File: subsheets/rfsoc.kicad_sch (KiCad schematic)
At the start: 27 parts, among them U1 nRF54L15-QFXX, U2 ADXL367BCCZ-RL7, X2 32MHz

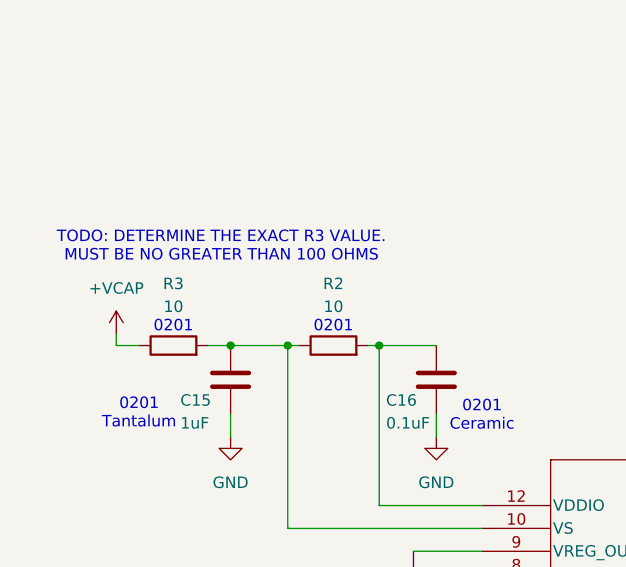
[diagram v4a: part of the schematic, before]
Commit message: changed resistor to ferrite bead for accel power filtering
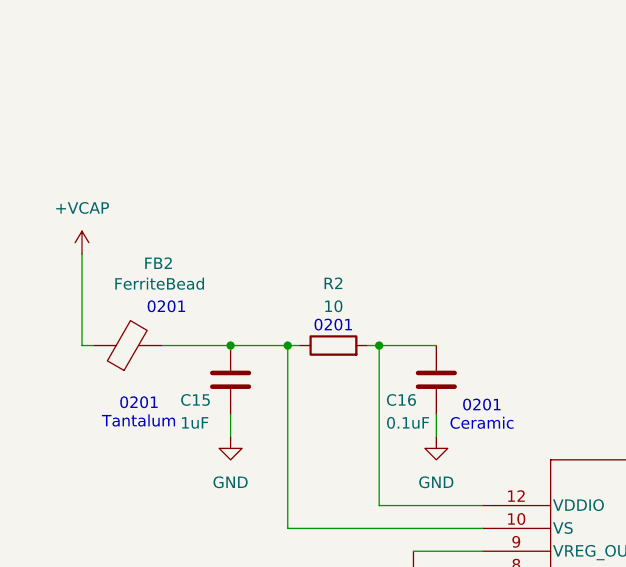
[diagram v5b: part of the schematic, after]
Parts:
- removed R3: 10, symbol Device:R
- added FB2: FerriteBead, symbol Device:FerriteBead
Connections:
- net +VCAP: now also FB2.1
- net at C15.1, R2.1, U2.10 (VS): now also FB2.2
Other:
- note removed: "TODO: DETERMINE THE EXACT R3 VALUE. MUST BE NO GREATER THAN 100 OHMS"
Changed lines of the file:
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@@
 	(wire
 		(pts
-			(xy 30.48 105.41) (xy 30.48 106.68)
+			(xy 26.67 96.52) (xy 26.67 106.68)
 		)
 		(stroke
@@
 	(wire
 		(pts
-			(xy 30.48 106.68) (xy 33.02 106.68)
+			(xy 26.67 106.68) (xy 27.94 106.68)
 		)
 		(stroke
@@
 	(wire
 		(pts
-			(xy 40.64 106.68) (xy 43.18 106.68)
+			(xy 35.56 106.68) (xy 43.18 106.68)
 		)
 		(stroke
@@
 		)
 	)
-	(text "0201\n"
+	(text "XTAL_2016\n"
 		(exclude_from_sim no)
-		(at 36.83 104.648 0)
+		(at 212.344 70.866 0)
 		(effects
 			(font
@@
 		)
 	)
-	(text "XTAL_2016\n"
+	(text "0201\n"
 		(exclude_from_sim no)
-		(at 212.344 70.866 0)
+		(at 259.08 43.688 0)
 		(effects
 			(font
@@
 	(text "0201\n"
 		(exclude_from_sim no)
-		(at 259.08 43.688 0)
+		(at 36.068 102.616 0)
 		(effects
 			(font
@@
 		)
 	)
-	(text "TODO: DETERMINE THE EXACT R3 VALUE. \nMUST BE NO GREATER THAN 100 OHMS\n"
-		(exclude_from_sim no)
-		(at 42.164 95.758 0)
-		(effects
-			(font
-				(size 1.27 1.27)
-			)
-		)
-	)
 	(text "0201\n"
 		(exclude_from_sim no)
@@
 	)
 	(symbol
-		(lib_id "Device:R")
-		(at 36.83 106.68 90)
-		(unit 1)
-		(exclude_from_sim no)
-		(in_bom yes)
-		(on_board yes)
-		(dnp no)
-		(property "Reference" "R3"
-			(at 36.83 99.822 90)
-			(effects
-				(font
-					(size 1.27 1.27)
-				)
-			)
-		)
-		(property "Value" "10"
-			(at 36.83 102.362 90)
-			(effects
-				(font
-					(size 1.27 1.27)
-				)
-			)
-		)
-		(property "Footprint" ""
-			(at 36.83 108.458 90)
-			(effects
-				(font
-					(size 1.27 1.27)
-				)
-				(hide yes)
-			)
-		)
-		(property "Datasheet" "~"
-			(at 36.83 106.68 0)
-			(effects
-				(font
-					(size 1.27 1.27)
-				)
-				(hide yes)
-			)
-		)
-		(property "Description" "Resistor"
-			(at 36.83 106.68 0)
-			(effects
-				(font
-					(size 1.27 1.27)
-				)
-				(hide yes)
-			)
-		)
-		(pin "1"
-		)
-		(pin "2"
-		)
-		(instances
-			(project "earworm_hardware"
-				(path "/881910d0-5a86-41d0-856d-d1bf2648669f/775ed5aa-f2a7-4007-b181-21772bd09852"
-					(reference "R3")
-					(unit 1)
-				)
-			)
-		)
-	)
-	(symbol
 		(lib_id "power:GND")
 		(at 204.47 85.09 0)
@@
 	)
 	(symbol
+		(lib_id "Device:FerriteBead")
+		(at 31.75 106.68 90)
+		(unit 1)
+		(exclude_from_sim no)
+		(in_bom yes)
+		(on_board yes)
+		(dnp no)
+		(property "Reference" "FB2"
+			(at 36.83 97.5869 90)
+			(effects
+				(font
+					(size 1.27 1.27)
+				)
+				(justify left)
+			)
+		)
+		(property "Value" "FerriteBead"
+			(at 40.386 99.8729 90)
+			(effects
+				(font
+					(size 1.27 1.27)
+				)
+				(justify left)
+			)
+		)
+		(property "Footprint" ""
+			(at 31.75 108.458 90)
+			(effects
+				(font
+					(size 1.27 1.27)
+				)
+				(hide yes)
+			)
+		)
+		(property "Datasheet" "~"
+			(at 31.75 106.68 0)
+			(effects
+				(font
+					(size 1.27 1.27)
+				)
+				(hide yes)
+			)
+		)
+		(property "Description" "Ferrite bead"
+			(at 31.75 106.68 0)
+			(effects
+				(font
+					(size 1.27 1.27)
+				)
+				(hide yes)
+			)
+		)
+		(pin "1"
+		)
+		(pin "2"
+		)
+		(instances
+			(project "earworm_hardware"
+				(path "/881910d0-5a86-41d0-856d-d1bf2648669f/775ed5aa-f2a7-4007-b181-21772bd09852"
+					(reference "FB2")
+					(unit 1)
+				)
+			)
+		)
+	)
+	(symbol
 		(lib_id "power:GND")
 		(at 68.58 139.7 0)
@@
 	(symbol
 		(lib_id "power:+1V0")
-		(at 30.48 105.41 0)
+		(at 26.67 96.52 0)
 		(unit 1)
 		(exclude_from_sim no)
@@
 		(fields_autoplaced yes)
 		(property "Reference" "#PWR021"
-			(at 30.48 109.22 0)
+			(at 26.67 100.33 0)
 			(effects
 				(font
@@
 		)
 		(property "Value" "+VCAP"
-			(at 30.48 100.33 0)
+			(at 26.67 91.44 0)
 			(effects
 				(font
@@
 		)
 		(property "Footprint" ""
-			(at 30.48 105.41 0)
+			(at 26.67 96.52 0)
 			(effects
 				(font
@@
 		)
 		(property "Datasheet" ""
-			(at 30.48 105.41 0)
+			(at 26.67 96.52 0)
 			(effects
 				(font
@@
 		)
 		(property "Description" "Power symbol creates a global label with name \"+1V0\""
-			(at 30.48 105.41 0)
+			(at 26.67 96.52 0)
 			(effects
 				(font

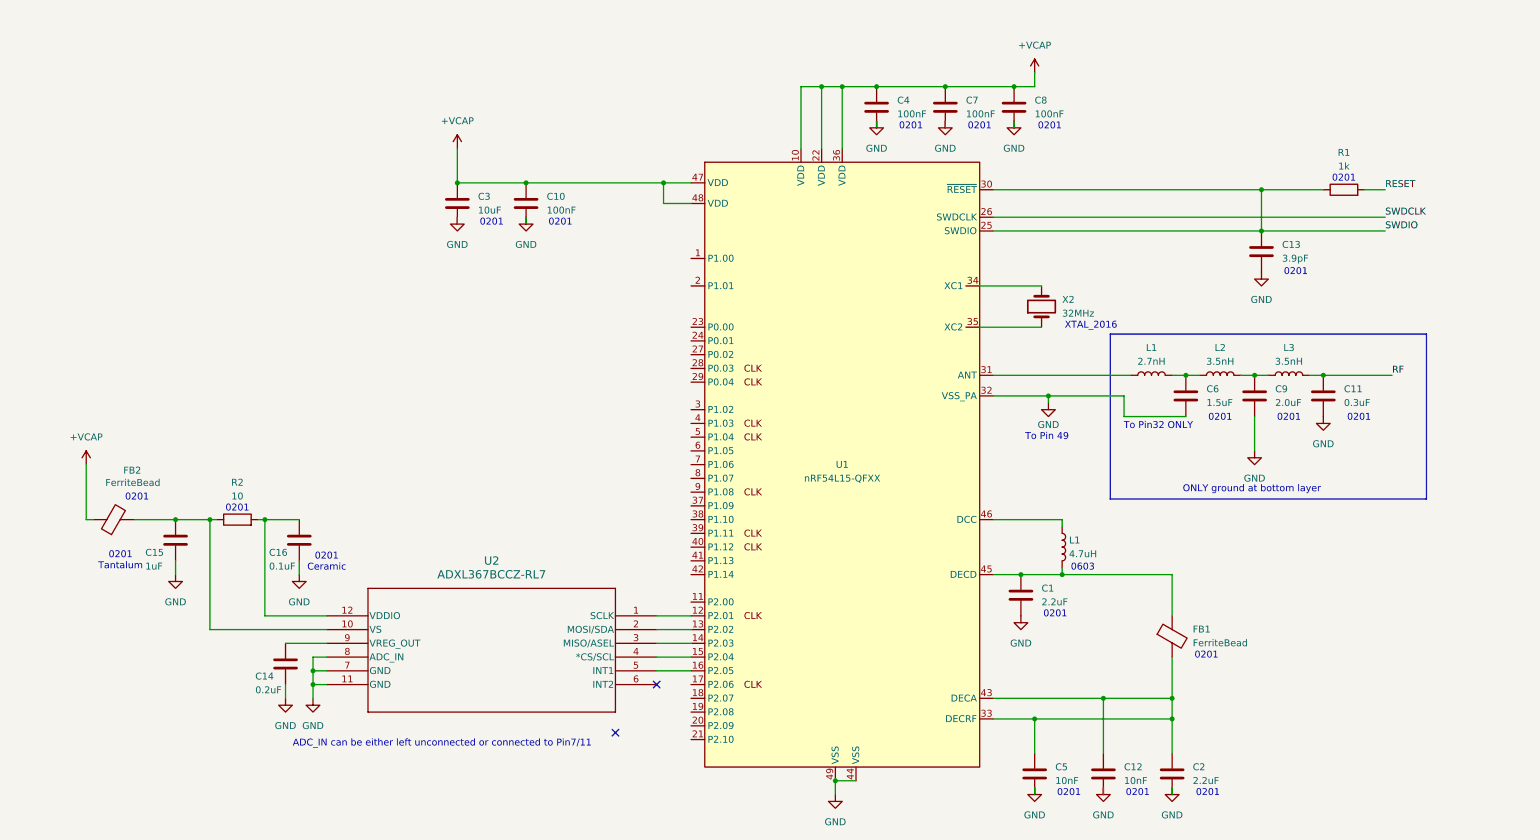
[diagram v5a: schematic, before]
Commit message: Added first draft of thermal energy harvesting chain. Need to run through ERC and fix errors
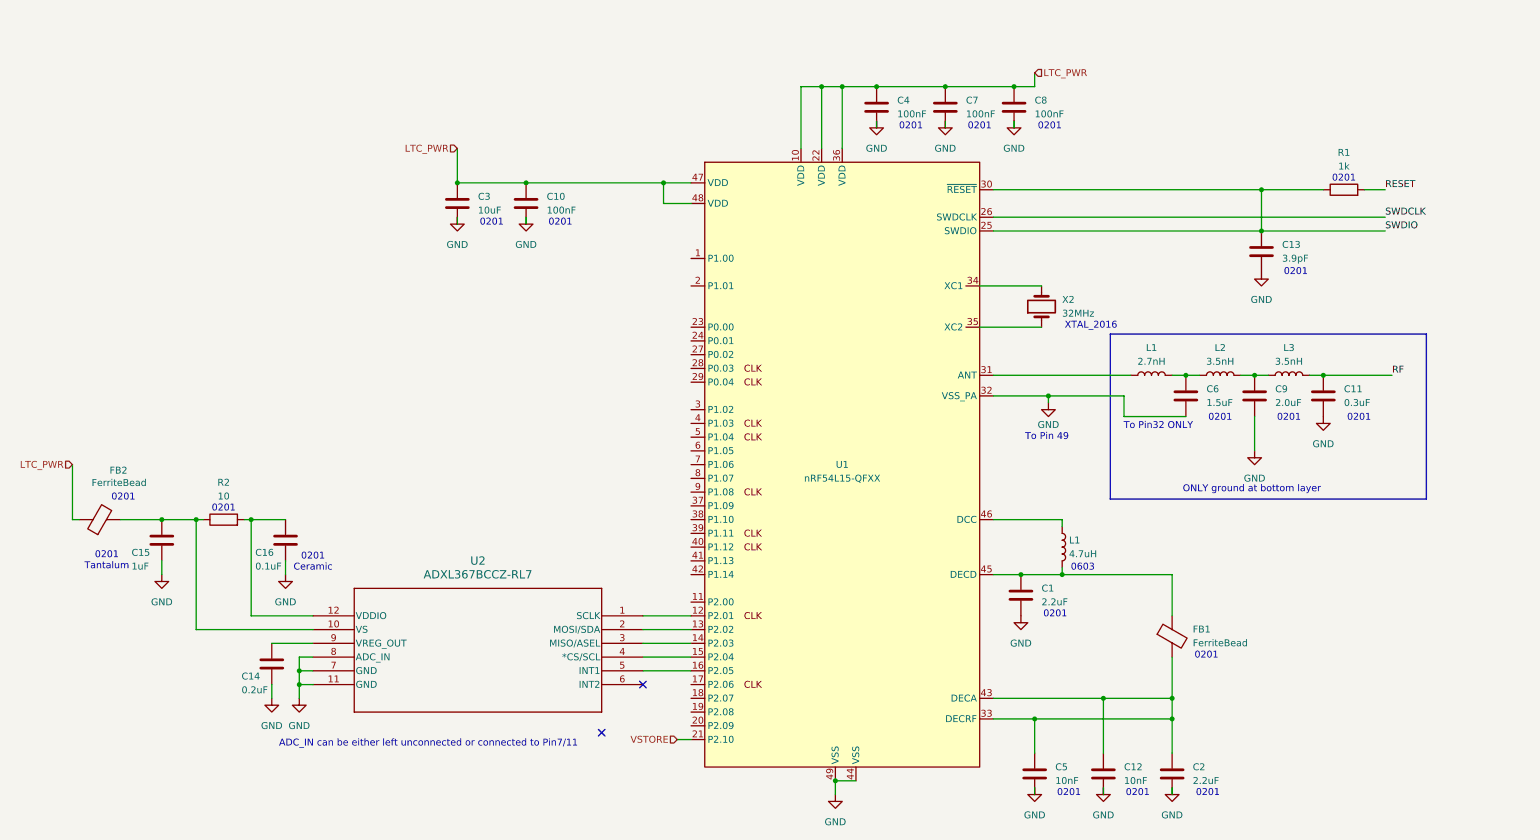
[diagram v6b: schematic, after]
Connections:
- net VSTORE: now reaches U1.21 (P2.10)
- net +VCAP renamed LTC_PWR
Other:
- moved on the sheet: C14, C15, C16, FB2, R2, U2

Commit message: Finished Schematic
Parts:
- removed C1: 2.2uF, symbol Device:C
- removed C2: 2.2uF, 0603, symbol Device:C
- removed C4, C7: 100nF, 0603, symbol Device:C
- removed C5: 10nF, 0603, symbol Device:C
- removed FB2: FerriteBead, symbol Device:FerriteBead
- removed L3: 3.5nH, symbol Device:L
- removed R1: 1k, symbol Device:R
- added C13, C9: 0.1uF, Capacitor_SMD:C_0603_1608Metric, symbol Device:C
- added C18: 10nF, Capacitor_SMD:C_0603_1608Metric, symbol Device:C
- added C19: 2.2uF, Capacitor_SMD:C_0603_1608Metric, symbol Device:C
- added C7: 1uF, Capacitor_SMD:C_0603_1608Metric_Pad1.08x0.95mm_HandSolder, symbol Device:C_Polarized
- added FB1: 75 @ 100MHz, Inductor_SMD:L_0603_1608Metric, symbol Device:FerriteBead
- added J2: Conn_01x05, Connector_PinHeader_1.00mm:PinHeader_1x05_P1.00mm_Vertical, symbol Connector_Generic:Conn_01x05
- added L4: 3.5nH, Inductor_SMD:L_0201_0603Metric, symbol Device:L
- added R2: 1k, Resistor_SMD:R_0603_1608Metric_Pad0.98x0.95mm_HandSolder, symbol Device:R_US
- C10: value 100nF -> 0.1uF; footprint 0603 -> Capacitor_SMD:C_0603_1608Metric; Part (none) -> CL10B104KB8NNNC; Tolerance (none) -> 10%; Voltage (none) -> 50V
- C11: renamed from C3; footprint 0603 -> Capacitor_SMD:C_0603_1608Metric; Part (none) -> CL10A106KQ8NNNC; Tolerance (none) -> 10%; Voltage (none) -> 6.3V
- C12: value 10nF -> 0.1uF; footprint 0603 -> Capacitor_SMD:C_0603_1608Metric; Part (none) -> CL10B104KB8NNNC; Tolerance (none) -> 10%; Voltage (none) -> 50V
- C14: value 0.2uF -> 0.1uF; footprint (none) -> Capacitor_SMD:C_0603_1608Metric; Part (none) -> CL10B104KB8NNNC; Tolerance (none) -> 10%; Voltage (none) -> 50V
- C15: value 1uF -> 2.2uF; footprint (none) -> Capacitor_SMD:C_0603_1608Metric; Part (none) -> CL10A225KO8NNNC; Tolerance (none) -> 10%; Voltage (none) -> 16V
- C16: value 0.1uF -> 10nF; footprint (none) -> Capacitor_SMD:C_0603_1608Metric; Part (none) -> CL10B103KB8NNNC; Tolerance (none) -> 10%; Voltage (none) -> 50V
- C17: renamed from C13; value 3.9pF -> 4pF; footprint (none) -> Capacitor_SMD:C_0603_1608Metric; Part (none) -> CL10C040CB8NNNC; Tolerance (none) -> 6.25%; Voltage (none) -> 50V
- C20: renamed from C6; value 1.5uF -> 1.5pF; footprint 0603 -> Capacitor_SMD:C_0201_0603Metric; Part (none) -> GJM0335C1E1R5WB01D
- C21: renamed from C9; value 2.0uF -> 2.0pF; footprint 0603 -> Capacitor_SMD:C_0201_0603Metric; Part (none) -> GJM0335C1E2R0WB01D
- C22: renamed from C11; value 0.3uF -> 0.3pF; footprint 0603 -> Capacitor_SMD:C_0201_0603Metric; Part (none) -> GJM0335C1ER30WB01D
- C8: value 100nF -> 0.22uF; footprint 0603 -> Capacitor_SMD:C_0603_1608Metric; Part (none) -> CL10B224KO8NNNC; Tolerance (none) -> 10%; Voltage (none) -> 16V
- FB2: renamed from FB1; value FerriteBead -> 120 @ 100MHz; footprint (none) -> Inductor_SMD:L_0603_1608Metric; Part (none) -> BLM18KG121TN1D
- L1: footprint (none) -> Inductor_SMD:L_0603_1608Metric; Current (none) -> 620mA; Part (none) -> LQM18PN4R7MFRL; Tolerance (none) -> 20%
- L2: renamed from L1; footprint (none) -> Inductor_SMD:L_0201_0603Metric; Part (none) -> LQP03HQ2N7B02D
- L3: renamed from L2; footprint (none) -> Inductor_SMD:L_0201_0603Metric; Part (none) -> LQP03HQ3N5B02D
- R1: renamed from R2; footprint (none) -> Resistor_SMD:R_0603_1608Metric; symbol Device:R -> Device:R_US; Part (none) -> ERJ-3EKF10R0V; Tolerance (none) -> 1%; Wattage (none) -> 1/10W
- U2: footprint (none) -> earworm:LGA-CC-12-4
- X1: renamed from X2; footprint (none) -> Crystal:Crystal_SMD_2016-4Pin_2.0x1.6mm; symbol Device:Crystal -> Device:Crystal_GND24; Part (none) -> ECS-320-8-37CKM; Stability (none) -> 10ppm; lc (none) -> 8pF
- renumbered U1 to U3
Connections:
- net GND: now also X1.2, X1.4, C13.2, C18.2, C19.2, C7.2, C9.2, J2.1 (Pin_1)
- net RF: now also L4.2
- net SWDIO: now also J2.4 (Pin_4); no longer C17.1, U3.30 (~{RESET})
- net at R1.2, U2.12 (VDDIO): now also C9.1; no longer C16.1
- net at U2.9 (VREG_OUT): now also C8.1; no longer C14.1
- net at R1.1, U2.10 (VS): now also C7.1, FB1.2; no longer C15.1
- net at FB2.2, U3.33 (DECRF), U3.43 (DECA): now also C16.1, C18.1, C19.1; no longer C12.1
- net at C21.1, L3.2: now also L4.1
- net at FB2.1, L1.2, U3.45 (DECD): now also C15.1
- net at U3.34 (XC1): now also X1.3; no longer X1.2
- net LTC_PWR renamed VDD
- net VDD: now also C12.1, C14.1, C13.1, FB1.1, J2.2 (Pin_2); no longer C8.1
- net SWDCLK renamed SWCLK
- net SWCLK: now also J2.5 (Pin_5)
- new net: C17.1, R2.1, U3.30 (~{RESET})
- new net NRST: J2.3 (Pin_3), R2.2
- no-connect marks 2 -> 26
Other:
- note added: "nRF Schematic From: https://docs.nordicsemi.com/bundle/ps_nrf54L15/page/chapters/ref_circuitry.html"
- note removed: "0201"
- note removed: "0201 Ceramic"
- note removed: "0201 Tantalum"
- note removed: "0603"
- note removed: "XTAL_2016"
- moved on the sheet: C11, C17, C20, C21, C22, FB2, L1

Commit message: Initial PCB Layout
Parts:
- added X1: 32.768 kHz, earworm:Crystal_SMD_ECS_2012-2Pin_2.0x1.2mm, symbol Device:Crystal
- C1: renamed from C10; footprint Capacitor_SMD:C_0603_1608Metric -> Capacitor_SMD:C_0402_1005Metric
- C10: renamed from C7; footprint Capacitor_SMD:C_0603_1608Metric_Pad1.08x0.95mm_HandSolder -> Capacitor_SMD:C_0402_1005Metric
- C11: renamed from C9; footprint Capacitor_SMD:C_0603_1608Metric -> Capacitor_SMD:C_0402_1005Metric
- C12: renamed from C15; footprint Capacitor_SMD:C_0603_1608Metric -> Capacitor_SMD:C_0402_1005Metric
- C13: renamed from C8; footprint Capacitor_SMD:C_0603_1608Metric -> Capacitor_SMD:C_0402_1005Metric
- C14: renamed from C16; footprint Capacitor_SMD:C_0603_1608Metric -> Capacitor_SMD:C_0402_1005Metric
- C15: renamed from C18; footprint Capacitor_SMD:C_0603_1608Metric -> Capacitor_SMD:C_0402_1005Metric
- C16: renamed from C19; footprint Capacitor_SMD:C_0603_1608Metric -> Capacitor_SMD:C_0402_1005Metric
- C2: renamed from C12; footprint Capacitor_SMD:C_0603_1608Metric -> Capacitor_SMD:C_0402_1005Metric
- C3: renamed from C14; footprint Capacitor_SMD:C_0603_1608Metric -> Capacitor_SMD:C_0402_1005Metric
- C5: renamed from C13; footprint Capacitor_SMD:C_0603_1608Metric -> Capacitor_SMD:C_0402_1005Metric
- C6: renamed from C17; footprint Capacitor_SMD:C_0603_1608Metric -> Capacitor_SMD:C_0402_1005Metric
- FB1, FB2: footprint Inductor_SMD:L_0603_1608Metric -> Inductor_SMD:L_0402_1005Metric
- R1: renamed from R2; footprint Resistor_SMD:R_0603_1608Metric_Pad0.98x0.95mm_HandSolder -> Resistor_SMD:R_0402_1005Metric
- R2: renamed from R1; footprint Resistor_SMD:R_0603_1608Metric -> Resistor_SMD:R_0402_1005Metric
- renumbered C11 to C4, C20 to C7, C21 to C8, C22 to C9, J2 to J1, L2 to L1, L3 to L2, L4 to L3, L1 to L4, X1 to X2
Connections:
- net at U3.1 (P1.00): now also X1.2
- net at U3.2 (P1.01): now also X1.1
- no-connect marks 26 -> 24
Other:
- note added: "Single Supply recommended decoupling circuitry"
- moved on the sheet: C1, C2, C3, C4, C5
